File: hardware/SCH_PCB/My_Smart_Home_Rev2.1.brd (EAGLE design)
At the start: 68.6 x 53.3 mm, 88 parts, among them J1 ISP0, J2 ISP1, J3 MICROUSB-5P, J4 JUMPER, J5 13F-60FGYDPNW2NL, Q1 CJ2302, SW2 SW-2, U1 ATMEGA8U2, U2 ATMEGAXX8-AU, U3 W5100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

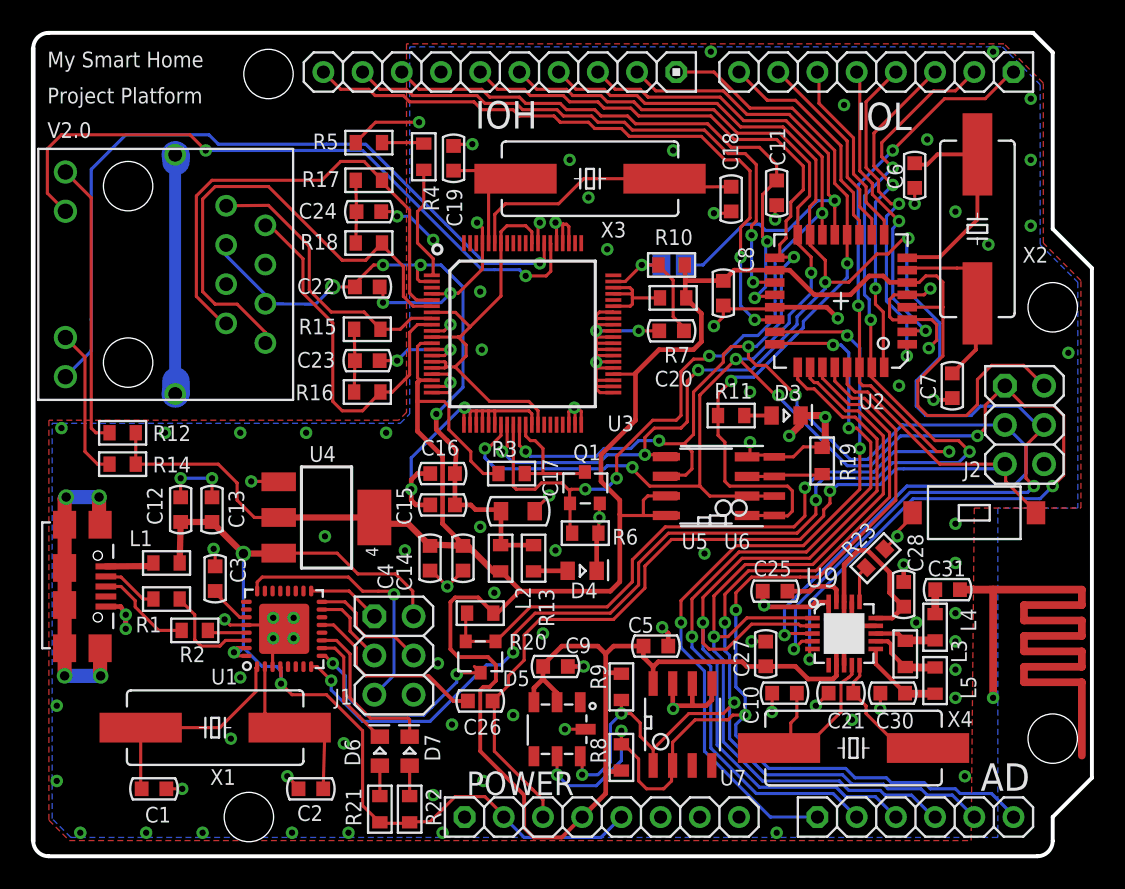
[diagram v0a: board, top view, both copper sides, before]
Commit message: Fix Hellduino V2.0 HW bugs, HW version update to V2.1
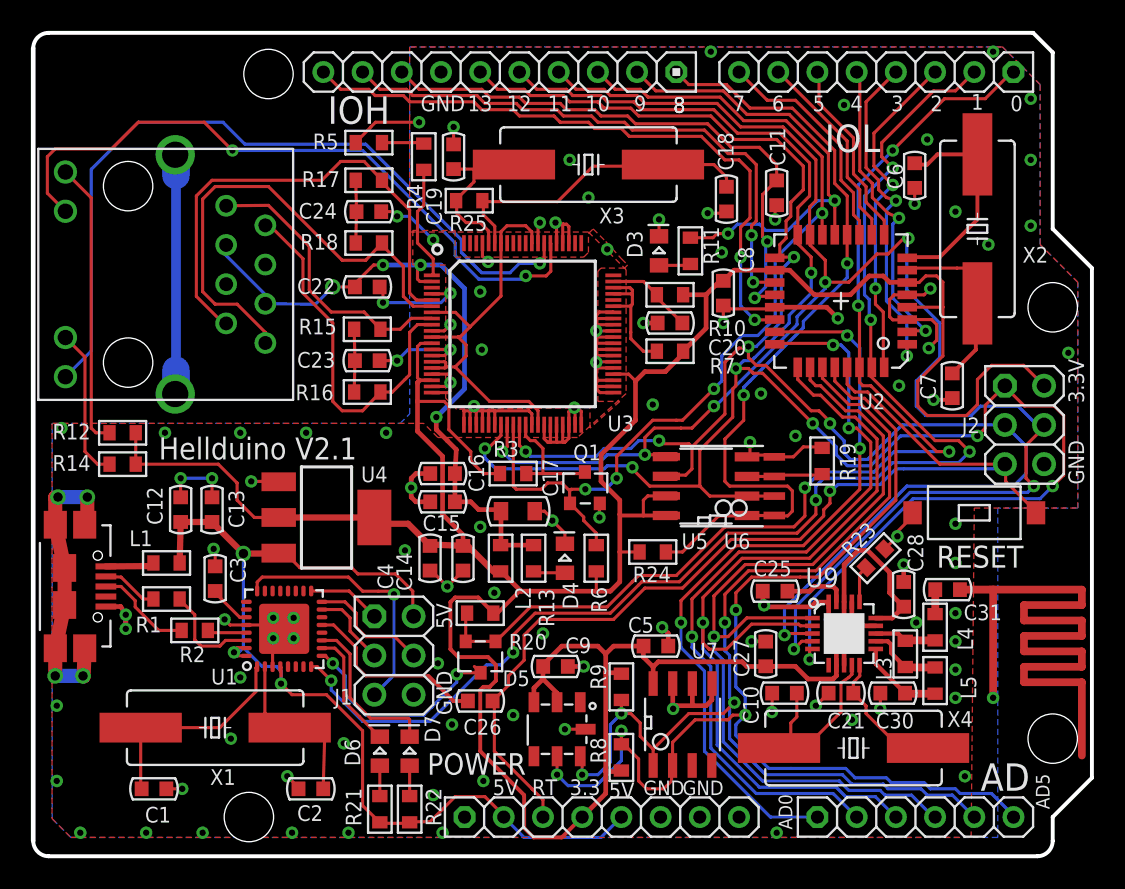
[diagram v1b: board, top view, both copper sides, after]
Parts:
- removed J4: JUMPER, Hell-Prototypes:SOLDER_JUMPER
- added R24: 10K, Hell-Prototypes:R0603
- added R25: 1M, Hell-Prototypes:R0603
- C31: value 33nF -> 1.5pF
- L4: value 8.2nH -> 3.9nH
- L5: value 8.2nH -> 2.7nH
- R10: value 10K -> 75K
- moved D3 13.5 mm to (40.5, 39.2), turned to 0 degrees
- moved R11 11.0 mm to (42.6, 39.2), turned to 270 degrees
- moved R7 3.46 mm to (41.2, 32.7)
- moved R10 1.93 mm to (41.2, 36.4)
- moved R6 1.77 mm to (36.5, 19.3), turned to 90 degrees
- moved D4 1.38 mm to (34.4, 19.3), turned to 0 degrees
- moved X3 0.92 mm to (36.0, 44.8)
- moved C20 0.52 mm to (41.2, 34.5)
- moved C18 0.30 mm to (44.9, 42.6)
- moved C15 0.20 mm to (26.5, 23.0)
- moved R3 0.10 mm to (31.1, 24.8)
- moved C19 0.10 mm to (27.2, 45.3)
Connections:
- net AD2 renamed AD2/NRF_CSN
- net AD3 renamed AD3/NRF_CE
- removed net IO8: IOH.1, R11.1, U2.12, U5.1, U6.1
- new net IO8/W25_SS: IOH.1, R24.2, U2.12, U5.1, U6.1
- net +3V3: now also R24.1, R6.1
- net ETH_RESET: no longer J4.1
- net GND: now also U3.34, U3.35, U3.36, U3.37; no longer R6.1
- net IO9: now also R11.1; no longer J4.2
- net N$3: now also R25.2
- net N$5: now also R25.1
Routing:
- net IO8/W25_SS: track 0.00 -> 52.8 mm, vias 0 -> 2
- net IO8: track 47.7 -> 0.00 mm, vias 2 -> 0
- net GND: track 221.1 -> 207.4 mm, vias 121 -> 119
- net ETH_RESET: track 9.64 -> 5.69 mm, vias 1 -> 0
- net N$4: track 6.55 -> 8.96 mm
- net N$3: track 18.8 -> 20.8 mm
- net SPDLED: track 49.0 -> 50.6 mm
- net MOSI_1: track 115.8 -> 114.3 mm
- net N$26: track 16.8 -> 15.5 mm
- net IO9: track 31.8 -> 30.7 mm, vias 1 -> 2
- net LINKLED: track 43.3 -> 44.3 mm
- net NRST_1: track 68.8 -> 68.0 mm
- net IO0: track 73.8 -> 72.9 mm
- net IO1: track 87.0 -> 86.2 mm
- net N$5: track 9.99 -> 10.7 mm
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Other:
- board text added: "3.3"
- board text added: "3.3V"
- board text added: "AD0"
- board text added: "AD5"
- board text added: "Hellduino V2.1"
- board text added: "RT"
- board text removed: "My Smart Home"
- board text removed: "Project Platform"
- board text removed: "V2.0"
